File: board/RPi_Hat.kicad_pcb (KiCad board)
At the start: 2 copper layers, 65 x 56.5 mm, 46 parts, among them IC1 ATMEGA328-A, IC2 RFM69HW, J1 RPi_GPIO, P1 FTDI_CONN_01X06, P10 SW_CONN, P11 BATT_IN, P12 CONN_01X01, P13 ICSP, P2 D8, P3 A0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

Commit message: changed FTDI to UART
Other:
- board text added: "UART"
- board text removed: "FTDI Port"
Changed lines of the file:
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@@
     (mod_text_size 1 1)
     (mod_text_width 0.15)
-    (pad_size 1.75 1.75)
-    (pad_drill 1)
+    (pad_size 1.2 0.9)
+    (pad_drill 0)
     (pad_to_mask_clearance 0)
     (aux_axis_origin 0 0)
@@
     (effects (font (size 1 1) (thickness 0.2)))
   )
-  (gr_text "FTDI Port" (at 136 62.05 90) (layer F.SilkS)
+  (gr_text UART (at 136.2 61.65 90) (layer F.SilkS)
     (effects (font (size 1 1) (thickness 0.2)))
   )

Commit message: upped the via pad anualar ring from 7.8thou to 11.8thou (+0.1mm)
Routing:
- net GND: track 87.3 -> 91.7 mm
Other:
- net class ANT: via_dia 1.2 -> 1.4
- net class BUS: via_dia 1.2 -> 1.4
- net class Default: via_dia 1 -> 1.2

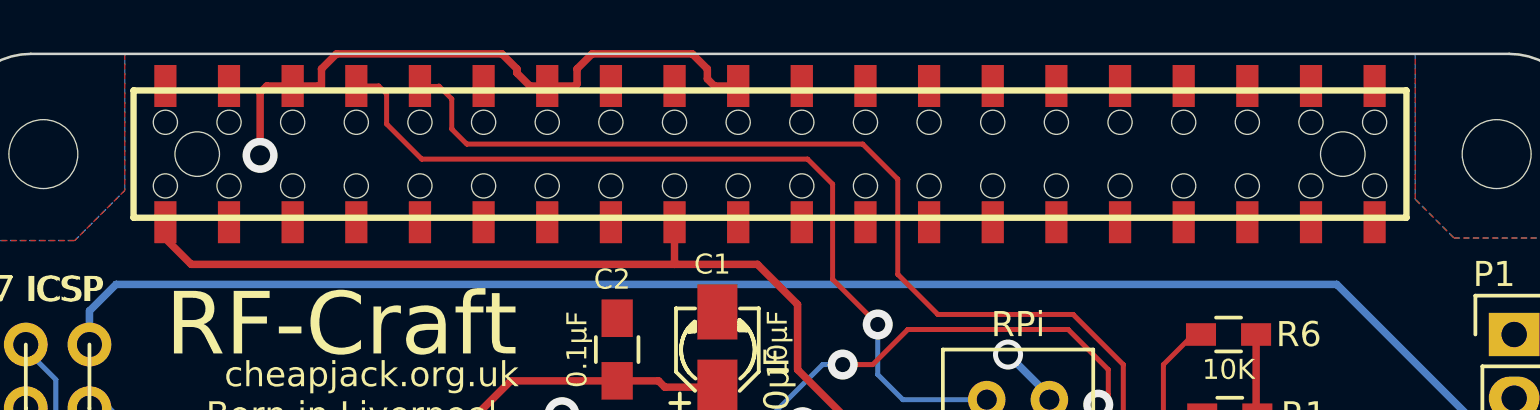
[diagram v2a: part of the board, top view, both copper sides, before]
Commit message: moved to double sided rpi header footprint
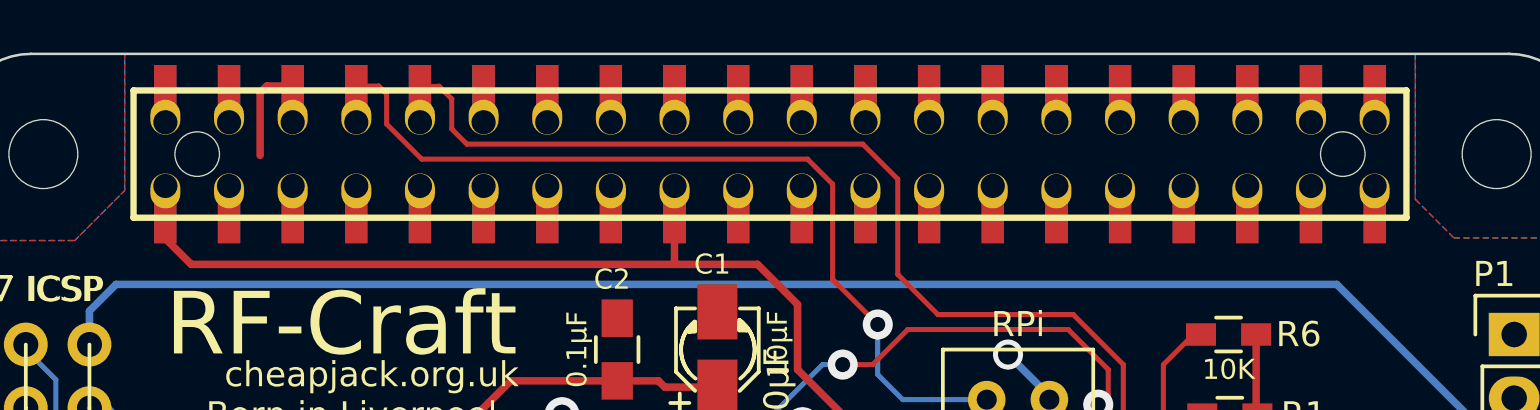
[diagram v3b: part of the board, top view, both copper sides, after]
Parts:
- J1: footprint cloudmaker:Samtec_HLE-120-02-XXX-DV-BE-XX-XX -> local:Samtec_HLE-120-02-XXX-DV-BE-XX-XX_DOUBLE
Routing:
- net V3.3_PI: track 41.8 -> 47.6 mm
- net TX_PI: track 34.4 -> 37.3 mm
- net RX_PI: track 47.0 -> 49.9 mm
- net Net-(J1-Pad7): track 0.00 -> 2.90 mm
- net Net-(J1-Pad5): track 0.00 -> 2.90 mm
- net Net-(J1-Pad40): track 0.00 -> 2.90 mm
- net Net-(J1-Pad4): track 0.00 -> 2.90 mm
- net Net-(J1-Pad38): track 0.00 -> 2.90 mm
- net Net-(J1-Pad37): track 0.00 -> 2.90 mm
- net Net-(J1-Pad36): track 0.00 -> 2.90 mm
- net Net-(J1-Pad35): track 0.00 -> 2.90 mm
- net Net-(J1-Pad33): track 0.00 -> 2.90 mm
- net Net-(J1-Pad32): track 0.00 -> 2.90 mm
- net Net-(J1-Pad31): track 0.00 -> 2.90 mm
- net Net-(J1-Pad3): track 0.00 -> 2.90 mm
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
